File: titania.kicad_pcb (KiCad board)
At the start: 2 copper layers, 83.8 x 40.6 mm, 27 parts, among them CON1 BARREL_JACK, P1 CONN_01X16, P2 CONN_01X16, P3 CONN_01X16, P4 CONN_01X16, P5 CONN_01X06, SW1 SW_PUSH, U1 LD1117S33TR, U2 PIC24FJ1024GB610, Y1 Crystal

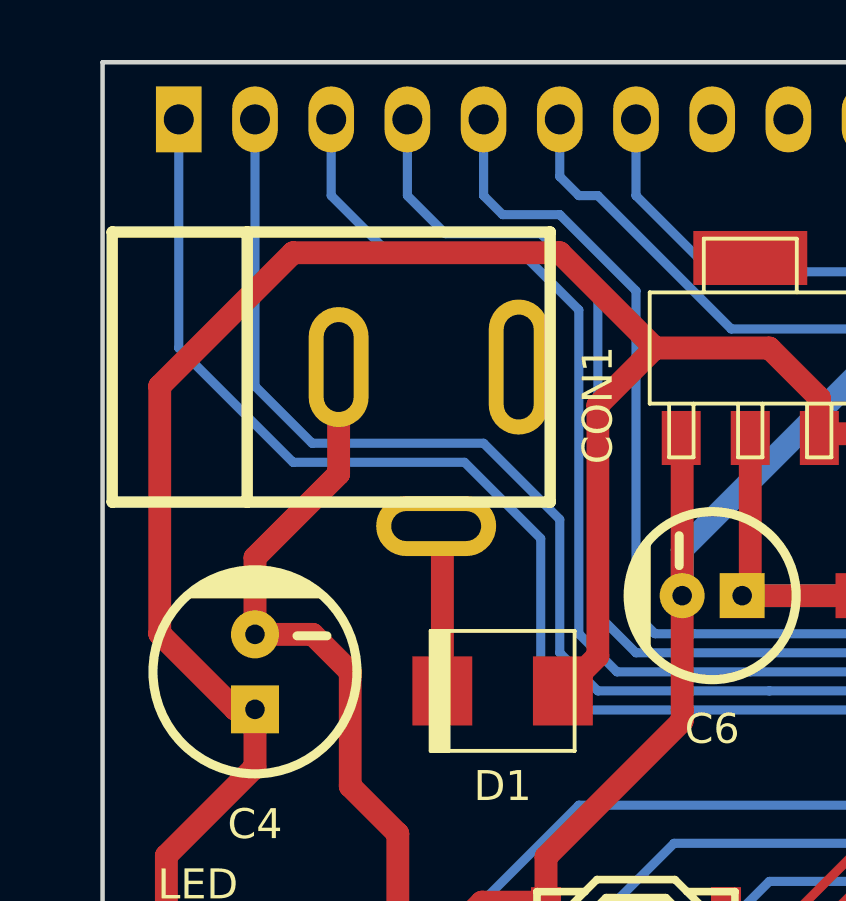
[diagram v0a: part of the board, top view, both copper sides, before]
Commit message: entrada usb energia
Signed-off-by: cuki2 <mauricio@krebs.com.br>
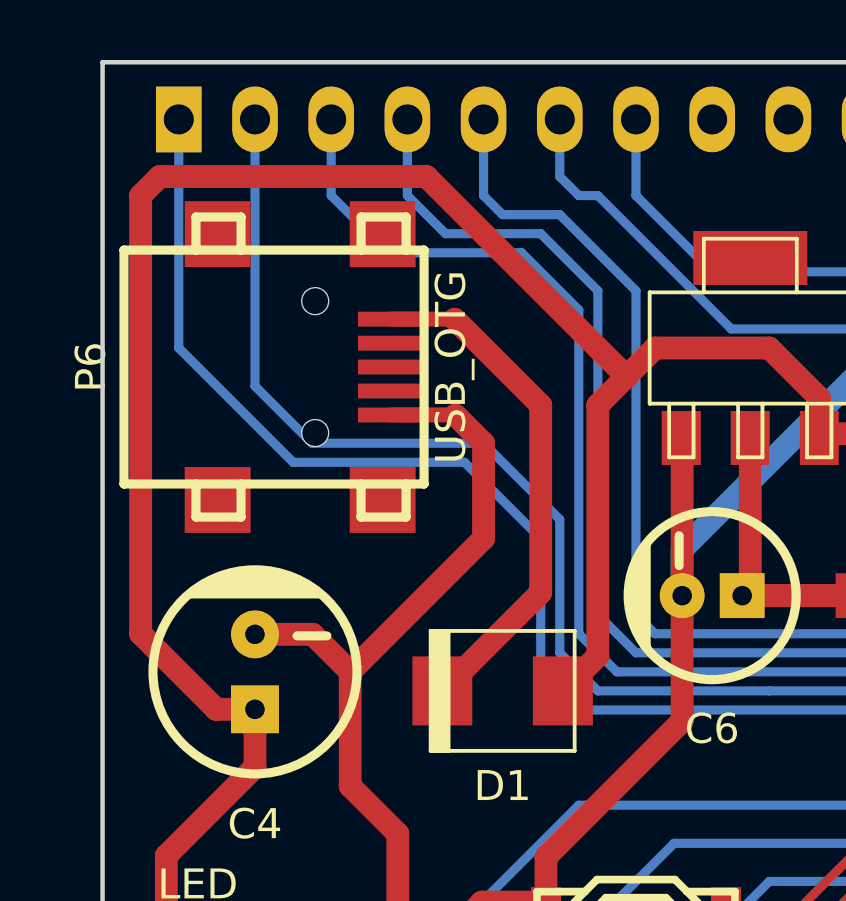
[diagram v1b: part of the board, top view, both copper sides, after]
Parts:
- removed CON1: BARREL_JACK, w_conn_misc:dc_socket
- added P6: USB_OTG, w_conn_pc:conn_usb_B_mini_smd, F.Cu at (76.8, 48.3)
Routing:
- net Net-(D1-Pad2): track 5.58 -> 17.1 mm
- net Net-(C4-Pad1): track 64.7 -> 71.2 mm
- net GND: track 200.1 -> 203.0 mm

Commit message: usb host
Signed-off-by: cuki2 <mauricio@krebs.com.br>
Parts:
- added C13: 100nF, w_smd_cap:c_0805, F.Cu at (125.5, 64.8)
- added C14: 470uF 16V, w_capacitors:CP_8x11.5mm, F.Cu at (137.7, 57.7)
- added C15: 100nF, w_smd_cap:c_0805, F.Cu at (131.6, 62.2)
- added C16: 150uF 6.3V, w_smd_cap:c_tant_C, F.Cu at (127.5, 50.8)
- added C17: 0.1uF 3.3V, w_smd_cap:c_0402, F.Cu at (122.4, 51.6)
- added CON1: BARREL_JACK, w_conn_misc:dc_socket, F.Cu at (76.7, 47.8)
- added F1: F_Small, MF-MSMF050-2:FUSM4632X85, F.Cu at (138.9, 69.1)
- added U3: LD1117S50TR, w_smd_trans:sot223, F.Cu at (130.3, 69.3)
- C2, C3: footprint w_smd_cap:c_0805 -> w_smd_cap:c_0603
- C4: value 470uF 25V -> 470uF 50V; footprint w_capacitors:CP_6.3x7mm -> w_capacitors:CP_12.5x15mm
- C6: footprint w_capacitors:CP_5x7mm -> w_capacitors:CP_8x11.5mm
- D1: footprint w_smd_diode:do214aa -> w_smd_diode:do214ac
- Y1: footprint w_crystal:crystal_hc-49%2fsmd -> w_crystal:crystal_smd_5x3.2mm
- moved P6 75.2 mm to (149.6, 67.3), turned to 90 degrees
- moved R3 25.7 mm to (145.3, 44.7)
- moved C1 25.5 mm to (100.3, 65.3), turned to 45 degrees
- moved P5 19.1 mm to (151.6, 51.1), turned to 270 degrees
- moved C11 11.4 mm to (87.9, 49.3), turned to 270 degrees
- moved C3 6.14 mm to (117.1, 46.2), turned to 270 degrees
- moved C2 6.14 mm to (109.0, 46.2), turned to 270 degrees
- moved C4 5.08 mm to (79.2, 62.5)
- moved D1 4.67 mm to (87.6, 55.6), turned to 90 degrees
- moved C6 4.26 mm to (95.5, 57.1)
- moved R2 4.07 mm to (79.8, 71.4)
- moved D2 4.07 mm to (74.2, 71.4)
- moved SW1 3.30 mm to (92.2, 68.1)
- moved C12 2.70 mm to (121.2, 50.3)
- moved Y1 0.76 mm to (113.0, 47.8)
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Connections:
- net Net-(C4-Pad1) renamed VCC
- D1 pad 2: Net-(D1-Pad2) -> Net-(CON1-Pad1)
- P1 pad 7: /L7 -> GND
- P1 pad 9: /L9 -> GND
- P4 pad 12: /L37 -> +3.3V
- P4 pad 13: /L36 -> +3.3V
- P4 pad 14: /L35 -> Net-(P4-Pad14)
- P4 pad 15: /L34 -> +5V
- P4 pad 16: /L33 -> +5V
- P6 pad 1: Net-(D1-Pad2) -> /L34
- P6 pad 2: Net-(P6-Pad2) -> /L36
- P6 pad 3: Net-(P6-Pad3) -> /L37
- P6 pad 4: Net-(P6-Pad4) -> /L33
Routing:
- net GND: track 203.0 -> 306.2 mm, vias 10 -> 14
- net +5V: track 0.00 -> 59.7 mm
- net /L15: track 47.4 -> 83.2 mm
- net /MCLR: track 38.9 -> 70.1 mm, vias 0 -> 5
- net /L35: track 37.5 -> 7.60 mm, vias 1 -> 0
- net VCC: track 71.2 -> 98.7 mm, vias 0 -> 4
- net /L16: track 39.3 -> 60.2 mm, vias 1 -> 3
- net +3.3V: track 139.4 -> 160.1 mm, vias 7 -> 6
- net Net-(D1-Pad2): track 17.1 -> 0.00 mm
- net /L12: track 16.5 -> 29.9 mm, vias 0 -> 1
- net /L30: track 37.5 -> 50.2 mm, vias 1 -> 7
- net /L1: track 39.9 -> 52.3 mm, vias 0 -> 3
- net /L23: track 18.9 -> 30.5 mm
- net /L24: track 20.5 -> 31.7 mm, vias 1 -> 2
- net /L32: track 43.3 -> 54.0 mm, vias 2 -> 1
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- added copper zone on B.Cu, net GND
- added copper zone on F.Cu, net GND
